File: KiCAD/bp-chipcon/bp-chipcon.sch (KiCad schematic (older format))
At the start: 33 parts, among them J1 audio_out, J2 video_out, J4 KEYPAD connector, M1 BLUE_PILL, Q1 2N3904, Q2 2N3906, SW1 power, U1 74HC86N

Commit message: Modification to schematic
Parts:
- removed D1: 1N4148, symbol device:D
- added F1: 250ma, symbol device:Fuse_Small
- renumbered D2 to D1, D3 to D2, D4 to D3, J4 to J3
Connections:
- net 3.3V is gone; now on net 3.0V: C2.1, J3.5 (Pin_5)
- net at BT1.1 (+): now also F1.1; no longer SW1.1 (A)
- net 3.0V: now reaches SW1.2 (B)
- net +3.3V renamed +3.0V
- new net: F1.2, SW1.1 (A)
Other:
- note added: "2xAAA\nAlkaline"
- note added: "Vbat\n3 volt\n"
- note removed: "3xAAA\nNiMh"
- note removed: "Vbat\n4volt\n"
- moved on the sheet: SW1A
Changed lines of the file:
@@
 $EndComp
 $Comp
-L power:GND #PWR012
+L power:GND #PWR011
 U 1 1 5CD3805D
 P 7225 3425
-F 0 "#PWR012" H 7225 3175 50  0001 C CNN
+F 0 "#PWR011" H 7225 3175 50  0001 C CNN
 F 1 "GND" H 7230 3252 50  0000 C CNN
 F 2 "" H 7225 3425 50  0001 C CNN
@@
 PA2
 $Comp
-L device:D D3
+L device:D D2
 U 1 1 5CD389F6
 P 8675 1650
-F 0 "D3" H 8675 1434 50  0000 C CNN
+F 0 "D2" H 8675 1434 50  0000 C CNN
 F 1 "1N4148" H 8675 1525 50  0000 C CNN
 F 2 "" H 8675 1650 50  0001 C CNN
@@
 	9125 1650 9125 2050
 $Comp
-L device:D D2
+L device:D D1
 U 1 1 5CD39683
 P 8675 1300
-F 0 "D2" H 8675 1084 50  0000 C CNN
+F 0 "D1" H 8675 1084 50  0000 C CNN
 F 1 "1N4148" H 8675 1175 50  0000 C CNN
 F 2 "" H 8675 1300 50  0001 C CNN
@@
 $EndComp
 $Comp
-L power:GND #PWR014
+L power:GND #PWR012
 U 1 1 5CD83218
 P 9125 3500
-F 0 "#PWR014" H 9125 3250 50  0001 C CNN
+F 0 "#PWR012" H 9125 3250 50  0001 C CNN
 F 1 "GND" H 9130 3327 50  0000 C CNN
 F 2 "" H 9125 3500 50  0001 C CNN
@@
 	1    0    0    -1
 $EndComp
-Text Notes 850  1525 0    50   ~ 0
-3xAAA\nNiMh
+Text Notes 775  1525 0    50   ~ 0
+2xAAA\nAlkaline
 Text Notes 1200 1200 2    50   ~ 0
-Vbat\n4volt\n
+Vbat\n3 volt\n
 $Comp
 L switches:SW_DPST_x2 SW1
 U 1 1 5CD8ACF7
-P 1550 1250
-F 0 "SW1" H 1550 1485 50  0000 C CNN
-F 1 "power" H 1550 1394 50  0000 C CNN
-F 2 "" H 1550 1250 50  0001 C CNN
-F 3 "" H 1550 1250 50  0001 C CNN
-	1    1550 1250
-	1    0    0    -1
-$EndComp
-Wire Wire Line
-	1200 1250 1350 1250
-$Comp
-L device:D D1
-U 1 1 5CD8B0B6
-P 2000 1250
-F 0 "D1" H 2000 1034 50  0000 C CNN
-F 1 "1N4148" H 2000 1125 50  0000 C CNN
-F 2 "" H 2000 1250 50  0001 C CNN
-F 3 "" H 2000 1250 50  0001 C CNN
-	1    2000 1250
-	-1   0    0    1
-$EndComp
-Wire Wire Line
-	1750 1250 1850 1250
+P 1950 1250
+F 0 "SW1" H 1950 1485 50  0000 C CNN
+F 1 "power" H 1950 1394 50  0000 C CNN
+F 2 "" H 1950 1250 50  0001 C CNN
+F 3 "" H 1950 1250 50  0001 C CNN
+	1    1950 1250
+	1    0    0    -1
+$EndComp
 $Comp
 L power:GND #PWR07
@@
 $EndComp
 Text Label 2150 1250 0    50   ~ 0
-3.3V
+3.0V
 $Comp
 L device:CP C2
@@
 $EndComp
 $Comp
-L power:GND #PWR019
+L power:GND #PWR013
 U 1 1 5CDD9F18
 P 6325 4700
-F 0 "#PWR019" H 6325 4450 50  0001 C CNN
+F 0 "#PWR013" H 6325 4450 50  0001 C CNN
 F 1 "GND" H 6330 4527 50  0000 C CNN
 F 2 "" H 6325 4700 50  0001 C CNN
@@
 $EndComp
 $Comp
-L device:D D4
+L device:D D3
 U 1 1 5CDDA1BE
 P 7100 4650
-F 0 "D4" V 7054 4729 50  0000 L CNN
+F 0 "D3" V 7054 4729 50  0000 L CNN
 F 1 "1N4148" V 7145 4729 50  0000 L CNN
 F 2 "" H 7100 4650 50  0001 C CNN
@@
 $EndComp
 $Comp
-L power:GND #PWR020
+L power:GND #PWR014
 U 1 1 5CDDA4C5
 P 7100 5200
-F 0 "#PWR020" H 7100 4950 50  0001 C CNN
+F 0 "#PWR014" H 7100 4950 50  0001 C CNN
 F 1 "GND" H 7105 5027 50  0000 C CNN
 F 2 "" H 7100 5200 50  0001 C CNN
@@
 $EndComp
 Text Label 6325 3850 0    50   ~ 0
-+3.3V
++3.0V
 Wire Wire Line
 	6325 4150 6325 4250
@@
 $EndComp
 Text Label 6425 6225 2    50   ~ 0
-+3.3V
++3.0V
 Wire Wire Line
 	6575 4850 7100 4850
@@
 $EndSheet
 $Comp
-L power:GND #PWR0101
+L power:GND #PWR015
 U 1 1 5CE4EBEB
 P 1600 6175
-F 0 "#PWR0101" H 1600 5925 50  0001 C CNN
+F 0 "#PWR015" H 1600 5925 50  0001 C CNN
 F 1 "GND" H 1605 6002 50  0000 C CNN
 F 2 "" H 1600 6175 50  0001 C CNN
@@
 $EndComp
 Text Label 2225 5775 2    50   ~ 0
-3.3V
+3.0V
 Text Label 2225 6075 2    39   ~ 0
 GP_CLK
@@
 NoConn ~ 3825 2600
 Text Label 4825 2600 0    50   ~ 0
-+3.3V
-$Comp
-L conn:Conn_01x05_Female J4
++3.0V
+$Comp
+L conn:Conn_01x05_Female J3
 U 1 1 5CE593C3
 P 1400 5975
-F 0 "J4" H 1294 5550 50  0000 C CNN
+F 0 "J3" H 1294 5550 50  0000 C CNN
 F 1 "KEYPAD connector" H 1294 5641 50  0000 C CNN
 F 2 "" H 1400 5975 50  0001 C CNN
@@
 	1600 6175 2450 6175
 Connection ~ 1600 6175
+$Comp
+L device:Fuse_Small F1
+U 1 1 5CFC72E3
+P 1575 1250
+F 0 "F1" H 1575 1435 50  0000 C CNN
+F 1 "250ma" H 1575 1344 50  0000 C CNN
+F 2 "" H 1575 1250 50  0001 C CNN
+F 3 "" H 1575 1250 50  0001 C CNN
+	1    1575 1250
+	1    0    0    -1
+$EndComp
+Wire Wire Line
+	1200 1250 1475 1250
+Wire Wire Line
+	1675 1250 1750 1250
 $EndSCHEMATC

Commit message: work on tvout
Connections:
- net GP_RX renamed GP_MOSI
- net GP_TX renamed GP_MISO
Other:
- note added: "2xAA\nAlkaline"
- note removed: "2xAAA\nAlkaline"
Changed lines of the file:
@@
 $EndComp
 Text Notes 775  1525 0    50   ~ 0
-2xAAA\nAlkaline
+2xAA\nAlkaline
 Text Notes 1200 1200 2    50   ~ 0
 Vbat\n3 volt\n
@@
 F3 "KEY_GND" U L 2450 6175 50
 F4 "KEY_CLK" I L 2450 6075 50
-F5 "KEY_IN" I L 2450 5875 50
-F6 "KEY_OUT" O L 2450 5975 50
+F5 "KEY_DIN" I L 2450 5875 50
+F6 "KEY_DOUT" O L 2450 5975 50
 $EndSheet
 $Comp
@@
 GP_CLK
 Text Label 2225 5875 2    39   ~ 0
-GP_RX
+GP_MOSI
 Text Label 2225 5975 2    39   ~ 0
-GP_TX
+GP_MISO
+Text Label 4825 4300 0    39   ~ 0
+GP_MOSI
 Text Label 4825 4200 0    39   ~ 0
-GP_TX
-Text Label 4825 4300 0    39   ~ 0
-GP_RX
+GP_MISO
 Text Label 4825 4400 0    39   ~ 0
 GP_CLK

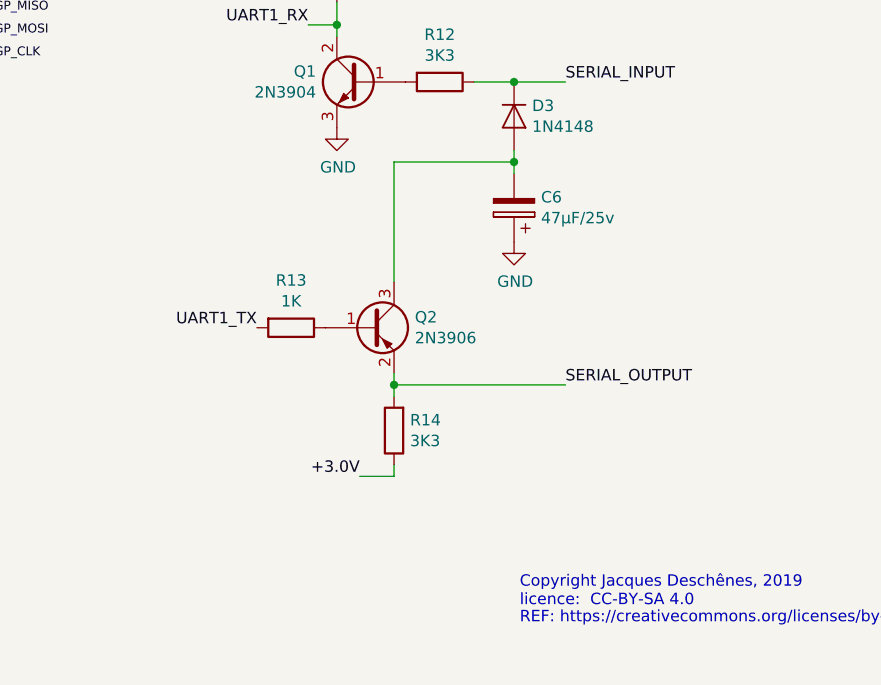
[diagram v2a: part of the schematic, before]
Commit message: corrected bug in serial port transmit circuit
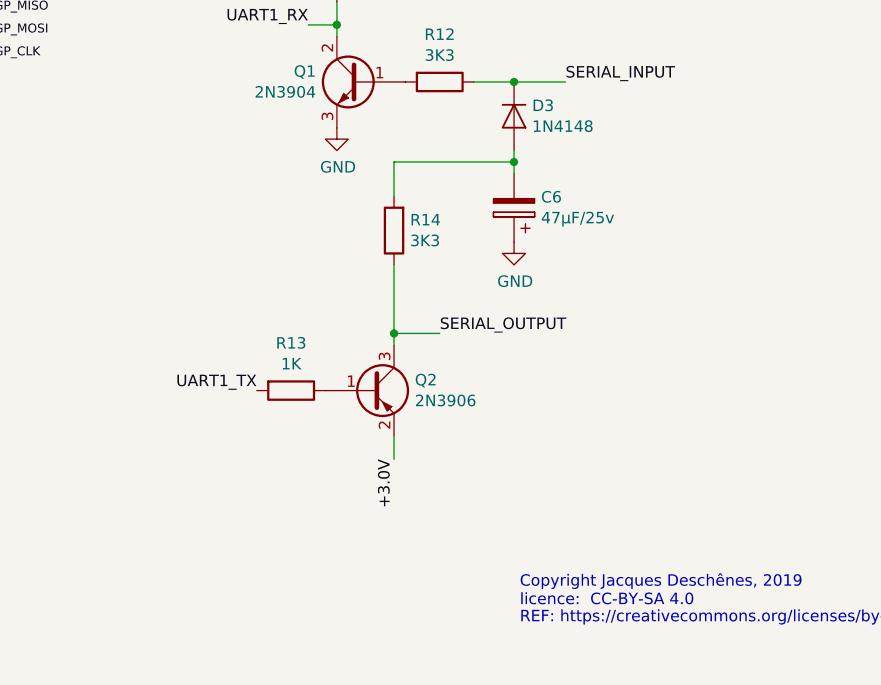
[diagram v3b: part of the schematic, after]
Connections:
- net +3.0V: now also Q2.2 (E); no longer R14.1
- net SERIAL_OUTPUT: now also Q2.3 (C), R14.1; no longer Q2.2 (E), R14.2
- net at C6.2, D3.2 (A): now also R14.2; no longer Q2.3 (C)
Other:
- moved on the sheet: Q2, R13, R14
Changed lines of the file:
@@
 Wire Wire Line
 	6925 4500 7100 4500
-Wire Wire Line
-	7100 4800 7100 4850
 $Comp
 L device:Q_PNP_BEC Q2
 U 1 1 5CDDAB0D
-P 6475 5575
-F 0 "Q2" H 6666 5621 50  0000 L CNN
-F 1 "2N3906" H 6666 5530 50  0000 L CNN
-F 2 "" H 6675 5675 50  0001 C CNN
-F 3 "" H 6475 5575 50  0001 C CNN
-	1    6475 5575
+P 6475 5850
+F 0 "Q2" H 6666 5896 50  0000 L CNN
+F 1 "2N3906" H 6666 5805 50  0000 L CNN
+F 2 "" H 6675 5950 50  0001 C CNN
+F 3 "" H 6475 5850 50  0001 C CNN
+	1    6475 5850
 	1    0    0    -1
 $EndComp
@@
 L device:R R14
 U 1 1 5CDDAC8F
-P 6575 6025
-F 0 "R14" H 6505 5979 50  0000 R CNN
-F 1 "3K3" H 6505 6070 50  0000 R CNN
-F 2 "" V 6505 6025 50  0001 C CNN
-F 3 "" H 6575 6025 50  0001 C CNN
-	1    6575 6025
+P 6575 5150
+F 0 "R14" H 6505 5104 50  0000 R CNN
+F 1 "3K3" H 6505 5195 50  0000 R CNN
+F 2 "" V 6505 5150 50  0001 C CNN
+F 3 "" H 6575 5150 50  0001 C CNN
+	1    6575 5150
 	-1   0    0    1
 $EndComp
-Connection ~ 7100 4850
-Wire Wire Line
-	7100 4850 7100 4900
-Wire Wire Line
-	6575 4850 6575 5375
 $Comp
 L device:R R13
 U 1 1 5CDDB9F7
-P 6125 5575
-F 0 "R13" V 5918 5575 50  0000 C CNN
-F 1 "1K" V 6009 5575 50  0000 C CNN
-F 2 "" V 6055 5575 50  0001 C CNN
-F 3 "" H 6125 5575 50  0001 C CNN
-	1    6125 5575
+P 6125 5850
+F 0 "R13" V 5918 5850 50  0000 C CNN
+F 1 "1K" V 6009 5850 50  0000 C CNN
+F 2 "" V 6055 5850 50  0001 C CNN
+F 3 "" H 6125 5850 50  0001 C CNN
+	1    6125 5850
 	0    1    1    0
 $EndComp
-Text Label 6425 6225 2    50   ~ 0
+Text Label 6575 6150 3    50   ~ 0
 +3.0V
-Wire Wire Line
-	6575 4850 7100 4850
 Wire Wire Line
 	6200 4250 6325 4250
@@
 Wire Wire Line
 	6325 4250 6325 4300
-Text Label 5975 5575 2    50   ~ 0
+Text Label 5975 5850 2    50   ~ 0
 UART1_TX
-Wire Wire Line
-	6575 6175 6575 6225
-Wire Wire Line
-	6575 6225 6425 6225
 Text Label 7325 4500 0    50   ~ 0
 SERIAL_INPUT
-Text Label 7325 5825 0    50   ~ 0
+Text Label 6775 5600 0    50   ~ 0
 SERIAL_OUTPUT
-Wire Wire Line
-	6575 5775 6575 5825
-Connection ~ 6575 5825
-Wire Wire Line
-	6575 5825 6575 5875
 Wire Wire Line
 	7100 4500 7325 4500
 Connection ~ 7100 4500
-Wire Wire Line
-	6575 5825 7325 5825
 Text Notes 7125 6800 0    50   ~ 0
 Copyright Jacques Deschênes, 2019\nlicence:  CC-BY-SA 4.0
@@
 Wire Wire Line
 	1675 1250 1750 1250
+Wire Wire Line
+	7100 4800 7100 4850
+Wire Wire Line
+	6575 5000 6575 4850
+Wire Wire Line
+	6575 4850 7100 4850
+Connection ~ 7100 4850
+Wire Wire Line
+	7100 4850 7100 4900
+Wire Wire Line
+	6575 6050 6575 6150
+Wire Wire Line
+	6575 5300 6575 5600
+Wire Wire Line
+	6575 5600 6775 5600
+Connection ~ 6575 5600
+Wire Wire Line
+	6575 5600 6575 5650
 $EndSCHEMATC
